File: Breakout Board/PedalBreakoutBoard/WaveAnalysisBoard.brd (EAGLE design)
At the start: 160 x 100 mm, 55 parts, among them IC1 LD1117V, IC2 MCP6004P, J1 NYS2152, J2 NYS2152, U1 OPA1652AID

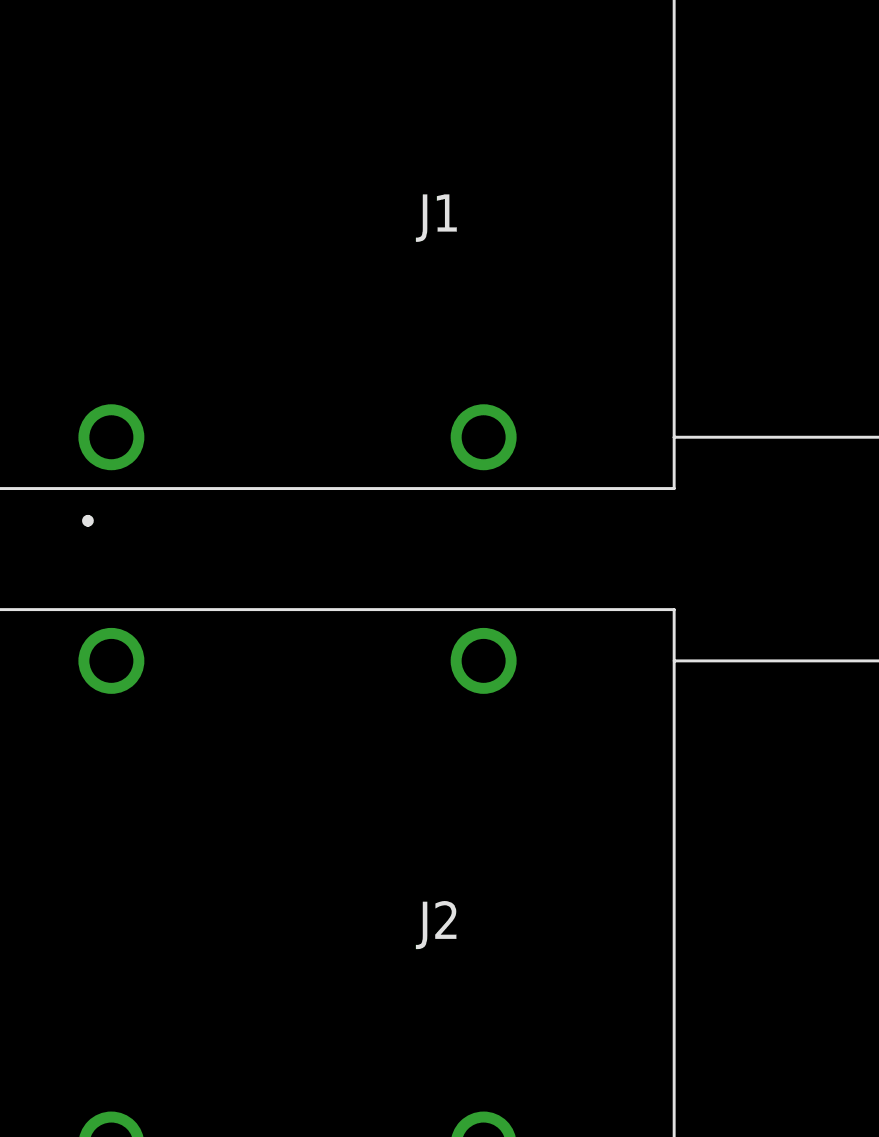
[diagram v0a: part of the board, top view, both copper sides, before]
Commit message: DP-97 - Update multi-effect with new grounding scheme
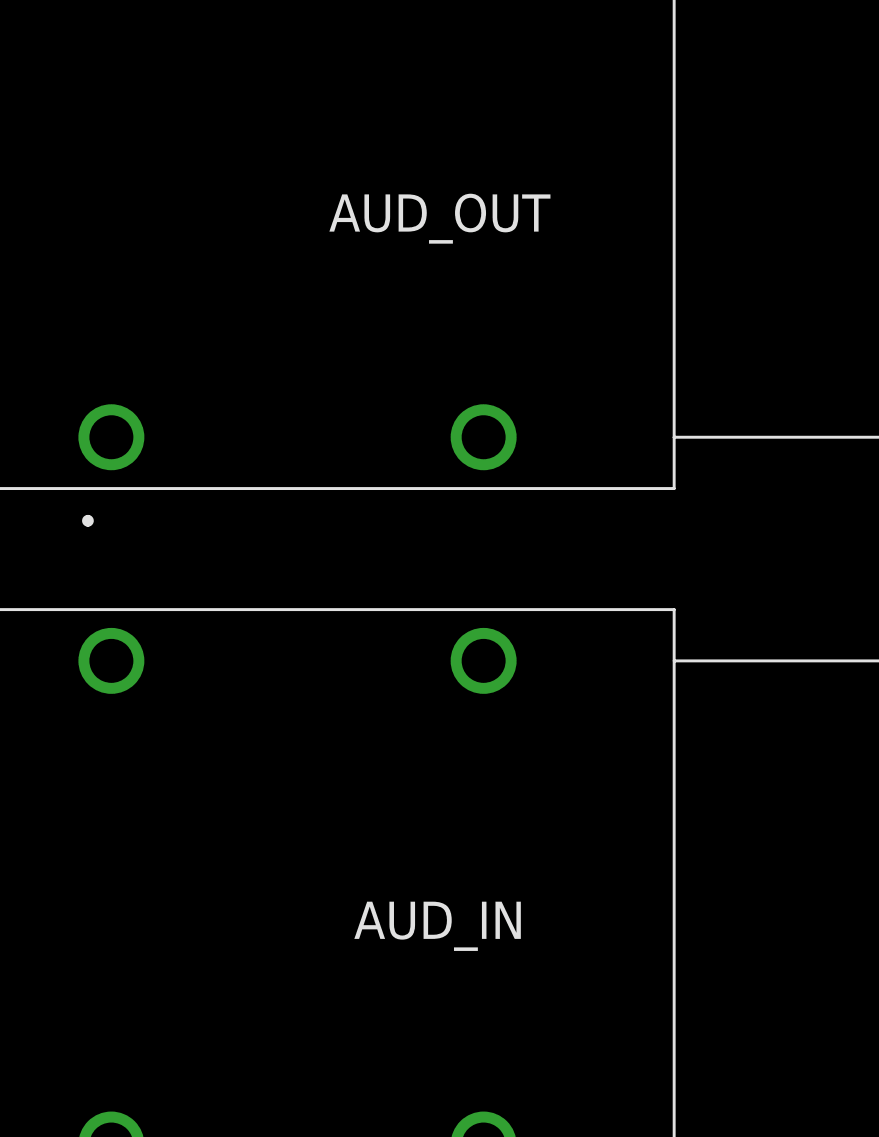
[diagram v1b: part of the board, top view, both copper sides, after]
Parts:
- renumbered J1 to AUD_OUT, J2 to AUD_IN
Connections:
- net AGND: now also C11.1, C3.2, C4.1, C6.2, IC1.1, PS1.1, PS1.3
- net GND: no longer C11.1, C3.2, C4.1, C6.2, IC1.1, PS1.1, PS1.3
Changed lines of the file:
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@@
 <attribute name="VENDOR" value="Texas Instruments" x="0" y="0" size="1.778" layer="27" display="off"/>
 </element>
-<element name="J1" library="SamacSys_Parts" package="NYS2152" value="NYS2152" x="-76.2" y="-20.32" smashed="yes">
+<element name="AUD_OUT" library="SamacSys_Parts" package="NYS2152" value="NYS2152" x="-76.2" y="-20.32" smashed="yes">
 <attribute name="DESCRIPTION" value="Phone Connectors 1/4&quot; MONO SWITCHED WITH CHROME NUT REAN" x="-76.2" y="-20.32" size="1.778" layer="27" display="off"/>
 <attribute name="HEIGHT" value="15.85mm" x="-76.2" y="-20.32" size="1.778" layer="27" display="off"/>
@@
 <attribute name="VALUE" x="-65" y="-12.67" size="1.27" layer="27" align="center"/>
 </element>
-<element name="J2" library="SamacSys_Parts" package="NYS2152" value="NYS2152" x="-76.2" y="-44.45" smashed="yes">
+<element name="AUD_IN" library="SamacSys_Parts" package="NYS2152" value="NYS2152" x="-76.2" y="-44.45" smashed="yes">
 <attribute name="DESCRIPTION" value="Phone Connectors 1/4&quot; MONO SWITCHED WITH CHROME NUT REAN" x="-76.2" y="-44.45" size="1.778" layer="27" display="off"/>
 <attribute name="HEIGHT" value="15.85mm" x="-76.2" y="-44.45" size="1.778" layer="27" display="off"/>
@@
 <contactref element="PWR" pad="1"/>
 <contactref element="C1" pad="2"/>
-<contactref element="IC1" pad="1"/>
-<contactref element="PS1" pad="1"/>
-<contactref element="PS1" pad="3"/>
-<contactref element="C11" pad="1"/>
-<contactref element="C4" pad="1"/>
-<contactref element="C3" pad="2"/>
-<contactref element="C6" pad="2"/>
 <contactref element="LED_GND" pad="1"/>
 <contactref element="D12" pad="P$1"/>
@@
 <wire x1="-22.86" y1="102.87" x2="-20.32" y2="102.87" width="0" layer="19" extent="1-1"/>
 <wire x1="-21.59" y1="95.25" x2="-20.32" y2="102.87" width="0" layer="19" extent="1-1"/>
-<wire x1="-17.907" y1="90.17" x2="-21.59" y2="95.25" width="0" layer="19" extent="1-1"/>
-<wire x1="-21.59" y1="83.82" x2="-17.907" y2="90.17" width="0" layer="19" extent="1-1"/>
-<wire x1="-27.813" y1="85.09" x2="-21.59" y2="83.82" width="0" layer="19" extent="1-1"/>
-<wire x1="-19.05" y1="76.2" x2="-21.59" y2="83.82" width="0" layer="19" extent="1-1"/>
-<wire x1="-24.13" y1="76.2" x2="-19.05" y2="76.2" width="0" layer="19" extent="1-1"/>
+<wire x1="-31.75" y1="106.68" x2="-22.86" y2="102.87" width="0" layer="19" extent="1-1"/>
+<wire x1="-31.75" y1="95.25" x2="-21.59" y2="95.25" width="0" layer="19" extent="1-1"/>
+<wire x1="-27.813" y1="85.09" x2="-31.75" y2="95.25" width="0" layer="19" extent="1-1"/>
 <wire x1="-36.957" y1="85.09" x2="-27.813" y2="85.09" width="0" layer="19" extent="1-1"/>
-<wire x1="-40.513" y1="85.09" x2="-36.957" y2="85.09" width="0" layer="19" extent="1-1"/>
-<wire x1="-45.72" y1="90.17" x2="-40.513" y2="85.09" width="0" layer="19" extent="1-1"/>
-<wire x1="-49.657" y1="85.09" x2="-45.72" y2="90.17" width="0" layer="19" extent="1-1"/>
-<wire x1="-55.88" y1="90.17" x2="-49.657" y2="85.09" width="0" layer="19" extent="1-1"/>
-<wire x1="-59.563" y1="85.09" x2="-55.88" y2="90.17" width="0" layer="19" extent="1-1"/>
-<wire x1="-66.04" y1="90.17" x2="-59.563" y2="85.09" width="0" layer="19" extent="1-1"/>
-<wire x1="-31.75" y1="106.68" x2="-22.86" y2="102.87" width="0" layer="19" extent="1-1"/>
+<wire x1="-45.72" y1="90.17" x2="-36.957" y2="85.09" width="0" layer="19" extent="1-1"/>
+<wire x1="-55.88" y1="90.17" x2="-45.72" y2="90.17" width="0" layer="19" extent="1-1"/>
+<wire x1="-66.04" y1="90.17" x2="-55.88" y2="90.17" width="0" layer="19" extent="1-1"/>
 <wire x1="-62.23" y1="99.06" x2="-66.04" y2="90.17" width="0" layer="19" extent="1-1"/>
 <wire x1="-64.77" y1="102.87" x2="-62.23" y2="99.06" width="0" layer="19" extent="1-1"/>
-<wire x1="-31.75" y1="95.25" x2="-21.59" y2="95.25" width="0" layer="19" extent="1-1"/>
 <wire x1="-76.2" y1="90.17" x2="-66.04" y2="90.17" width="0" layer="19" extent="1-1"/>
-<wire x1="-15.113" y1="53.34" x2="-19.05" y2="76.2" width="0" layer="19" extent="1-1"/>
+<wire x1="-15.113" y1="53.34" x2="-27.813" y2="85.09" width="0" layer="19" extent="1-1"/>
 </signal>
 <signal name="SPST1">
@@
 <contactref element="R8" pad="P$1"/>
 <contactref element="R10" pad="P$1"/>
-<wire x1="-49.53" y1="102.87" x2="-31.75" y2="99.06" width="0" layer="19" extent="1-1"/>
-<wire x1="-52.07" y1="102.87" x2="-49.53" y2="102.87" width="0" layer="19" extent="1-1"/>
-<wire x1="-52.07" y1="99.06" x2="-52.07" y2="102.87" width="0" layer="19" extent="1-1"/>
-<wire x1="-62.23" y1="95.25" x2="-52.07" y2="99.06" width="0" layer="19" extent="1-1"/>
-<wire x1="-65.913" y1="85.09" x2="-62.23" y2="95.25" width="0" layer="19" extent="1-1"/>
+<contactref element="IC1" pad="1"/>
+<contactref element="PS1" pad="1"/>
+<contactref element="PS1" pad="3"/>
+<contactref element="C11" pad="1"/>
+<contactref element="C4" pad="1"/>
+<contactref element="C3" pad="2"/>
+<contactref element="C6" pad="2"/>
+<wire x1="-21.59" y1="83.82" x2="-17.907" y2="90.17" width="0" layer="19" extent="1-1"/>
+<wire x1="-19.05" y1="76.2" x2="-21.59" y2="83.82" width="0" layer="19" extent="1-1"/>
+<wire x1="-24.13" y1="76.2" x2="-19.05" y2="76.2" width="0" layer="19" extent="1-1"/>
+<wire x1="-31.75" y1="99.06" x2="-17.907" y2="90.17" width="0" layer="19" extent="1-1"/>
+<wire x1="-40.513" y1="85.09" x2="-31.75" y2="99.06" width="0" layer="19" extent="1-1"/>
+<wire x1="-49.657" y1="85.09" x2="-40.513" y2="85.09" width="0" layer="19" extent="1-1"/>
+<wire x1="-53.213" y1="85.09" x2="-49.657" y2="85.09" width="0" layer="19" extent="1-1"/>
+<wire x1="-59.563" y1="85.09" x2="-53.213" y2="85.09" width="0" layer="19" extent="1-1"/>
+<wire x1="-65.913" y1="85.09" x2="-59.563" y2="85.09" width="0" layer="19" extent="1-1"/>
+<wire x1="-62.23" y1="95.25" x2="-59.563" y2="85.09" width="0" layer="19" extent="1-1"/>
 <wire x1="-66.1162" y1="74.295" x2="-65.913" y2="85.09" width="0" layer="19" extent="1-1"/>
 <wire x1="-71.0438" y1="74.295" x2="-66.1162" y2="74.295" width="0" layer="19" extent="1-1"/>
@@
 <wire x1="-68.58" y1="67.31" x2="-71.12" y2="67.31" width="0" layer="19" extent="1-1"/>
 <wire x1="-66.04" y1="59.69" x2="-68.58" y2="67.31" width="0" layer="19" extent="1-1"/>
-<wire x1="-53.213" y1="85.09" x2="-65.913" y2="85.09" width="0" layer="19" extent="1-1"/>
+<wire x1="-52.07" y1="99.06" x2="-62.23" y2="95.25" width="0" layer="19" extent="1-1"/>
+<wire x1="-52.07" y1="102.87" x2="-52.07" y2="99.06" width="0" layer="19" extent="1-1"/>
+<wire x1="-49.53" y1="102.87" x2="-52.07" y2="102.87" width="0" layer="19" extent="1-1"/>
 <wire x1="-82.55" y1="95.25" x2="-65.913" y2="85.09" width="0" layer="19" extent="1-1"/>
 <wire x1="-30.607" y1="5.08" x2="-66.04" y2="59.69" width="0" layer="19" extent="1-1"/>
